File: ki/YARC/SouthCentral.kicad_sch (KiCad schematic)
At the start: 9 parts, among them U104 74LS86, U83 74LS139, U84 74LS157, U85 74LS157, U86 74LS157, U87 74LS138, U88 74HC00, U89 74LS157, U90 74LS157

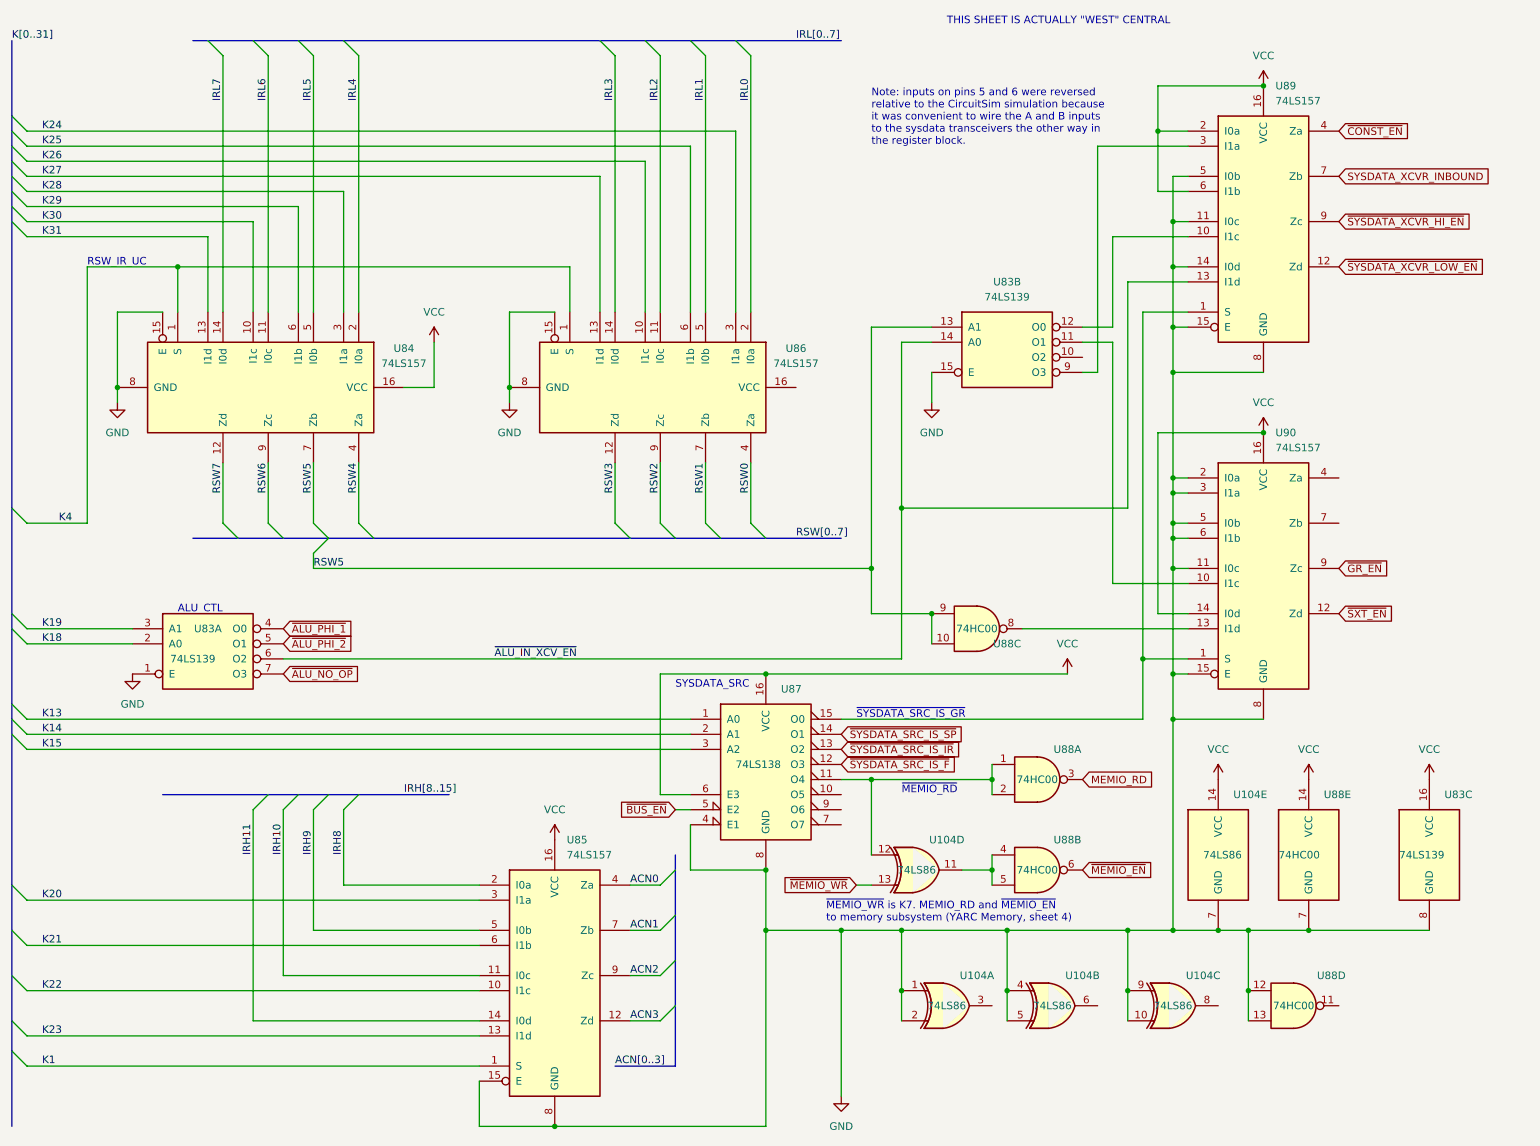
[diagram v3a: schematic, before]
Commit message: Ongoing fixes for ERC errors
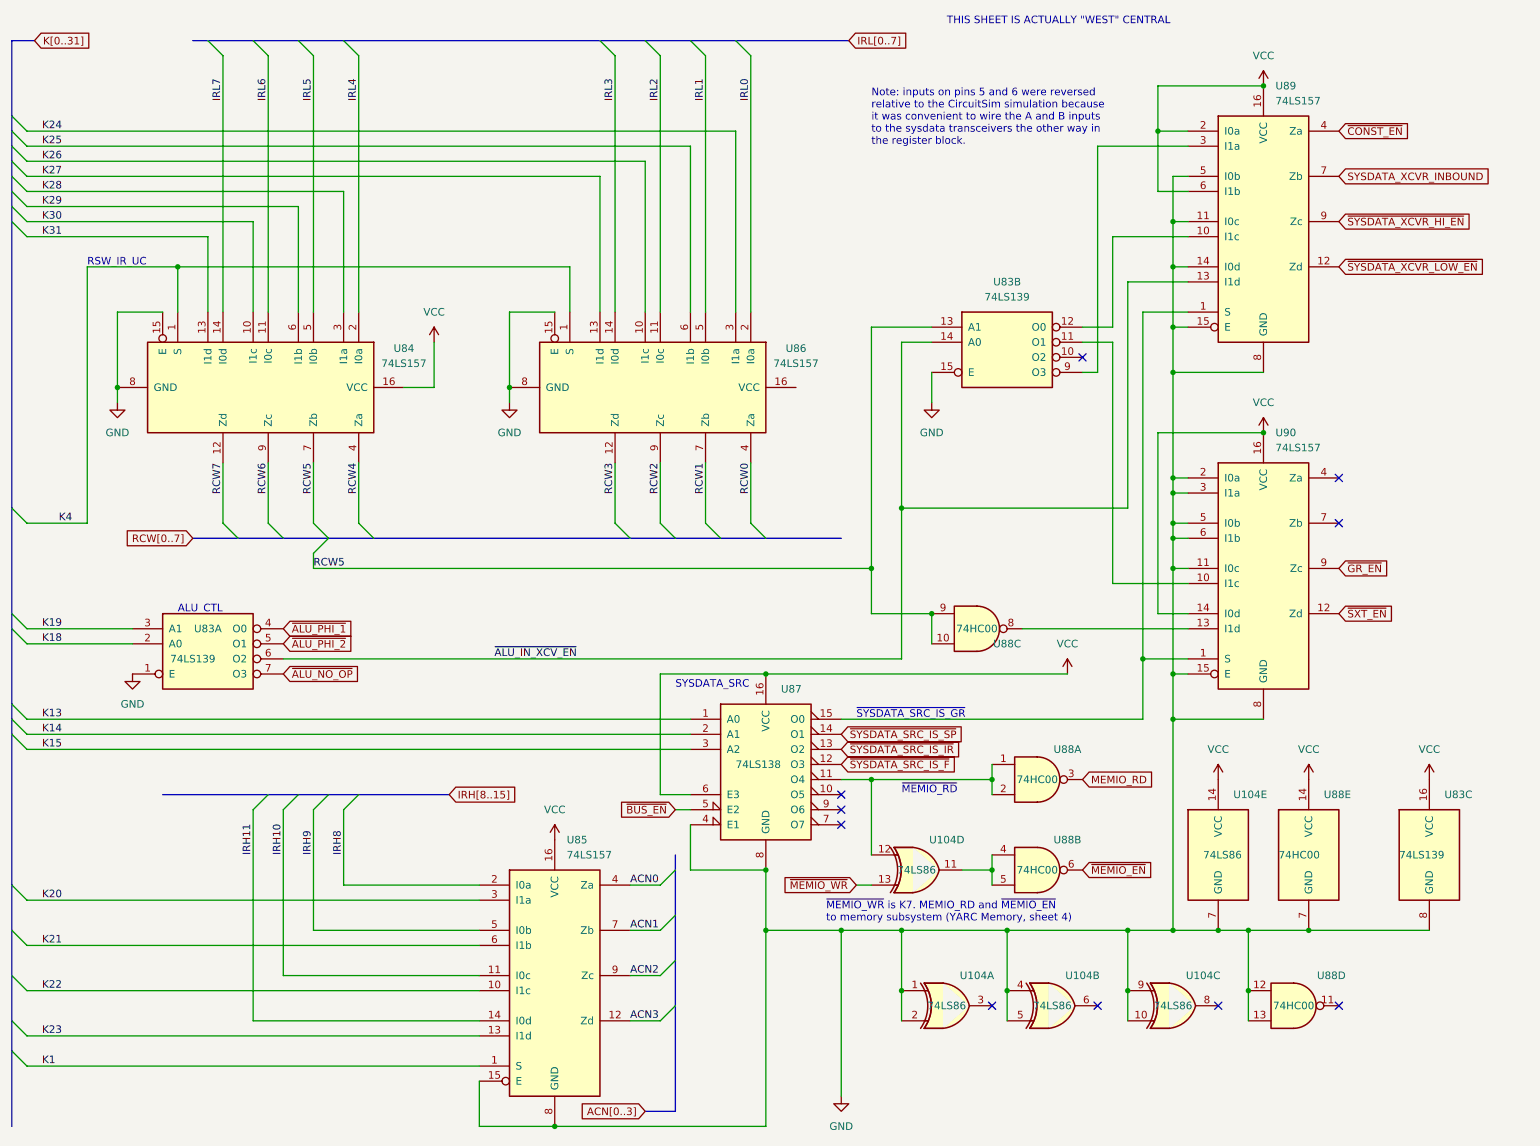
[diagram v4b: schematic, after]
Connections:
- net RSW0 renamed RCW0
- net RSW1 renamed RCW1
- net RSW2 renamed RCW2
- net RSW3 renamed RCW3
- net RSW4 renamed RCW4
- net RSW5 renamed RCW5
- net RSW6 renamed RCW6
- net RSW7 renamed RCW7
- no-connect marks 0 -> 10
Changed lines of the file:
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@@
   (junction (at 180.34 157.48) (diameter 0) (color 0 0 0 0)
   )
+  (no_connect (at 180.34 180.34))
+  (no_connect (at 238.76 91.44))
+  (no_connect (at 238.76 99.06))
+  (no_connect (at 195.58 71.12))
+  (no_connect (at 238.76 180.34))
+  (no_connect (at 154.94 147.32))
+  (no_connect (at 154.94 144.78))
+  (no_connect (at 198.12 180.34))
+  (no_connect (at 154.94 149.86))
+  (no_connect (at 218.44 180.34))
   (bus_entry (at 68.58 101.6) (size -2.54 -2.54)
     (stroke (width 0) (type default))
@@
     (stroke (width 0) (type default))
   )
-  (bus (pts (xy 116.84 190.5) (xy 127 190.5))
+  (bus (pts (xy 121.92 198.12) (xy 127 198.12))
     (stroke (width 0) (type default))
   )
@@
     (stroke (width 0) (type default))
   )
-  (bus (pts (xy 127 180.34) (xy 127 190.5))
+  (bus (pts (xy 127 180.34) (xy 127 198.12))
     (stroke (width 0) (type default))
   )
@@
     (stroke (width 0) (type default))
   )
+  (bus (pts (xy 15.24 17.78) (xy 19.05 17.78))
+    (stroke (width 0) (type default))
+  )
   (wire (pts (xy 33.02 78.74) (xy 33.02 76.2))
     (stroke (width 0) (type default))
@@
     (stroke (width 0) (type default))
   )
-  (bus (pts (xy 137.16 17.78) (xy 154.94 17.78))
+  (bus (pts (xy 137.16 17.78) (xy 156.21 17.78))
     (stroke (width 0) (type default))
   )
@@
     (effects (font (size 1.27 1.27)) (justify left bottom))
   )
-  (label "RSW6" (at 58.42 88.9 270) (fields_autoplaced)
+  (label "RCW6" (at 58.42 88.9 270) (fields_autoplaced)
     (effects (font (size 1.27 1.27)) (justify right bottom))
   )
@@
     (effects (font (size 1.27 1.27)) (justify left bottom))
   )
-  (label "RSW2" (at 124.46 88.9 270) (fields_autoplaced)
+  (label "RCW2" (at 124.46 88.9 270) (fields_autoplaced)
     (effects (font (size 1.27 1.27)) (justify right bottom))
   )
@@
   )
   (label "IRL0" (at 139.7 27.94 90) (fields_autoplaced)
-    (effects (font (size 1.27 1.27)) (justify left bottom))
-  )
-  (label "RSW[0..7]" (at 147.32 101.6 0) (fields_autoplaced)
     (effects (font (size 1.27 1.27)) (justify left bottom))
   )
@@
     (effects (font (size 1.27 1.27)) (justify right bottom))
   )
-  (label "K[0..31]" (at 15.24 17.78 0) (fields_autoplaced)
-    (effects (font (size 1.27 1.27)) (justify left bottom))
-  )
   (label "~{ALU_IN_XCV_EN}" (at 96.52 121.92 0) (fields_autoplaced)
     (effects (font (size 1.27 1.27)) (justify left bottom))
@@
     (effects (font (size 1.27 1.27)) (justify left bottom))
   )
-  (label "RSW0" (at 139.7 88.9 270) (fields_autoplaced)
+  (label "RCW0" (at 139.7 88.9 270) (fields_autoplaced)
     (effects (font (size 1.27 1.27)) (justify right bottom))
   )
@@
     (effects (font (size 1.27 1.27)) (justify left bottom))
   )
-  (label "ACN[0..3]" (at 116.84 190.5 0) (fields_autoplaced)
-    (effects (font (size 1.27 1.27)) (justify left bottom))
-  )
-  (label "RSW3" (at 116.84 88.9 270) (fields_autoplaced)
+  (label "RCW3" (at 116.84 88.9 270) (fields_autoplaced)
     (effects (font (size 1.27 1.27)) (justify right bottom))
   )
@@
     (effects (font (size 1.27 1.27)) (justify left bottom))
   )
-  (label "RSW7" (at 50.8 88.9 270) (fields_autoplaced)
+  (label "RCW7" (at 50.8 88.9 270) (fields_autoplaced)
     (effects (font (size 1.27 1.27)) (justify right bottom))
   )
@@
     (effects (font (size 1.27 1.27)) (justify left bottom))
   )
-  (label "IRH[8..15]" (at 81.28 144.78 0) (fields_autoplaced)
-    (effects (font (size 1.27 1.27)) (justify left bottom))
-  )
   (label "K24" (at 20.32 33.02 0) (fields_autoplaced)
     (effects (font (size 1.27 1.27)) (justify left bottom))
   )
-  (label "RSW1" (at 132.08 88.9 270) (fields_autoplaced)
+  (label "RCW1" (at 132.08 88.9 270) (fields_autoplaced)
     (effects (font (size 1.27 1.27)) (justify right bottom))
   )
@@
     (effects (font (size 1.27 1.27)) (justify left bottom))
   )
-  (label "RSW5" (at 66.04 88.9 270) (fields_autoplaced)
+  (label "RCW5" (at 66.04 88.9 270) (fields_autoplaced)
     (effects (font (size 1.27 1.27)) (justify right bottom))
   )
@@
     (effects (font (size 1.27 1.27)) (justify left bottom))
   )
-  (label "RSW4" (at 73.66 88.9 270) (fields_autoplaced)
+  (label "RCW4" (at 73.66 88.9 270) (fields_autoplaced)
     (effects (font (size 1.27 1.27)) (justify right bottom))
   )
@@
     (effects (font (size 1.27 1.27)) (justify left bottom))
   )
-  (label "IRL[0..7]" (at 147.32 17.78 0) (fields_autoplaced)
-    (effects (font (size 1.27 1.27)) (justify left bottom))
-  )
   (label "IRH11" (at 55.88 154.94 90) (fields_autoplaced)
     (effects (font (size 1.27 1.27)) (justify left bottom))
   )
-  (label "RSW5" (at 66.04 106.68 0) (fields_autoplaced)
+  (label "RCW5" (at 66.04 106.68 0) (fields_autoplaced)
     (effects (font (size 1.27 1.27)) (justify left bottom))
   )
@@
     )
   )
+  (global_label "IRL[0..7]" (shape input) (at 156.21 17.78 0) (fields_autoplaced)
+    (effects (font (size 1.27 1.27)) (justify left))
+    (property "Intersheetrefs" "${INTERSHEET_REFS}" (at 167.4201 17.78 0)
+      (effects (font (size 1.27 1.27)) (justify left) hide)
+    )
+  )
   (global_label "MEMIO_RD" (shape input) (at 195.58 142.24 0) (fields_autoplaced)
     (effects (font (size 1.27 1.27)) (justify left))
@@
     )
   )
+  (global_label "IRH[8..15]" (shape input) (at 88.9 144.78 0) (fields_autoplaced)
+    (effects (font (size 1.27 1.27)) (justify left))
+    (property "Intersheetrefs" "${INTERSHEET_REFS}" (at 101.622 144.78 0)
+      (effects (font (size 1.27 1.27)) (justify left) hide)
+    )
+  )
   (global_label "~{SYSDATA_XCVR_HI_EN}" (shape input) (at 238.76 48.26 0) (fields_autoplaced)
     (effects (font (size 1.27 1.27)) (justify left))
@@
     (property "Intersheetrefs" "${INTERSHEET_REFS}" (at 207.4274 157.4006 0)
       (effects (font (size 1.27 1.27)) (justify left) hide)
+    )
+  )
+  (global_label "RCW[0..7]" (shape input) (at 45.72 101.6 180) (fields_autoplaced)
+    (effects (font (size 1.27 1.27)) (justify right))
+    (property "Intersheetrefs" "${INTERSHEET_REFS}" (at 33.4214 101.6 0)
+      (effects (font (size 1.27 1.27)) (justify right) hide)
+    )
+  )
+  (global_label "ACN[0..3]" (shape input) (at 121.92 198.12 180) (fields_autoplaced)
+    (effects (font (size 1.27 1.27)) (justify right))
+    (property "Intersheetrefs" "${INTERSHEET_REFS}" (at 109.9237 198.12 0)
+      (effects (font (size 1.27 1.27)) (justify right) hide)
     )
   )
@@
       (effects (font (size 1.27 1.27)) (justify left) hide)
     )
+  )
+  (global_label "K[0..31]" (shape input) (at 19.05 17.78 0) (fields_autoplaced)
+    (effects (font (size 1.27 1.27)) (justify left))
+    (property "Intersheetrefs" "${INTERSHEET_REFS}" (at 29.8367 17.78 0)
+      (effects (font (size 1.27 1.27)) (justify left) hide)
+    )

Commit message: Ongoing schematic changes
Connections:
- net VCC: now also U86.16 (VCC)
- net RCW0 renamed DST:0
- net RCW1 renamed DST:1
- net RCW2 renamed DST:2
- net RCW3 renamed SRC2:0
- net RCW4 renamed SRC2:1
- net RCW5 renamed SRC2:2
- net RCW6 renamed SRC1:0
- net RCW7 renamed SRC1:1
- net ~{SYSDATA_SRC_IS_SP} renamed ~{SYSDATA_SRC_IS_A}

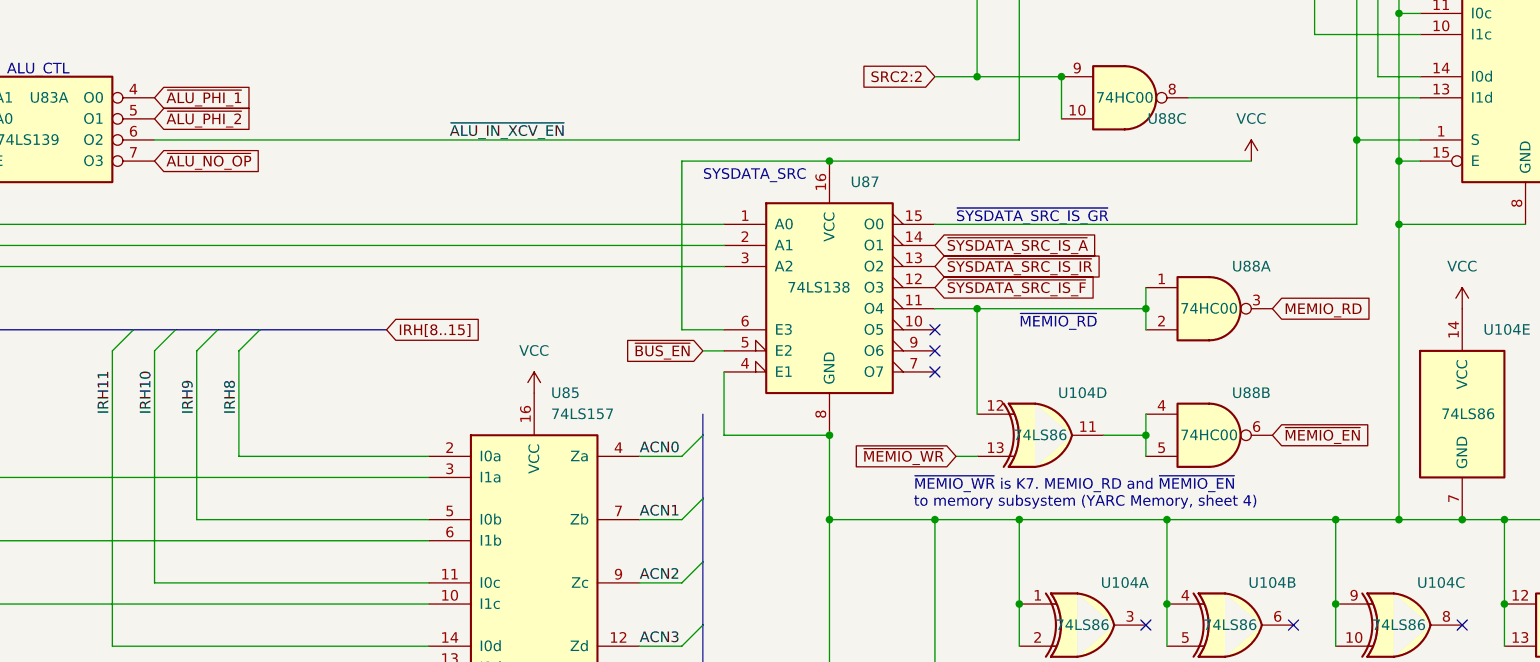
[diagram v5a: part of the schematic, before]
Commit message: Schematic for addressing unit is complete and all ERC violations addressed
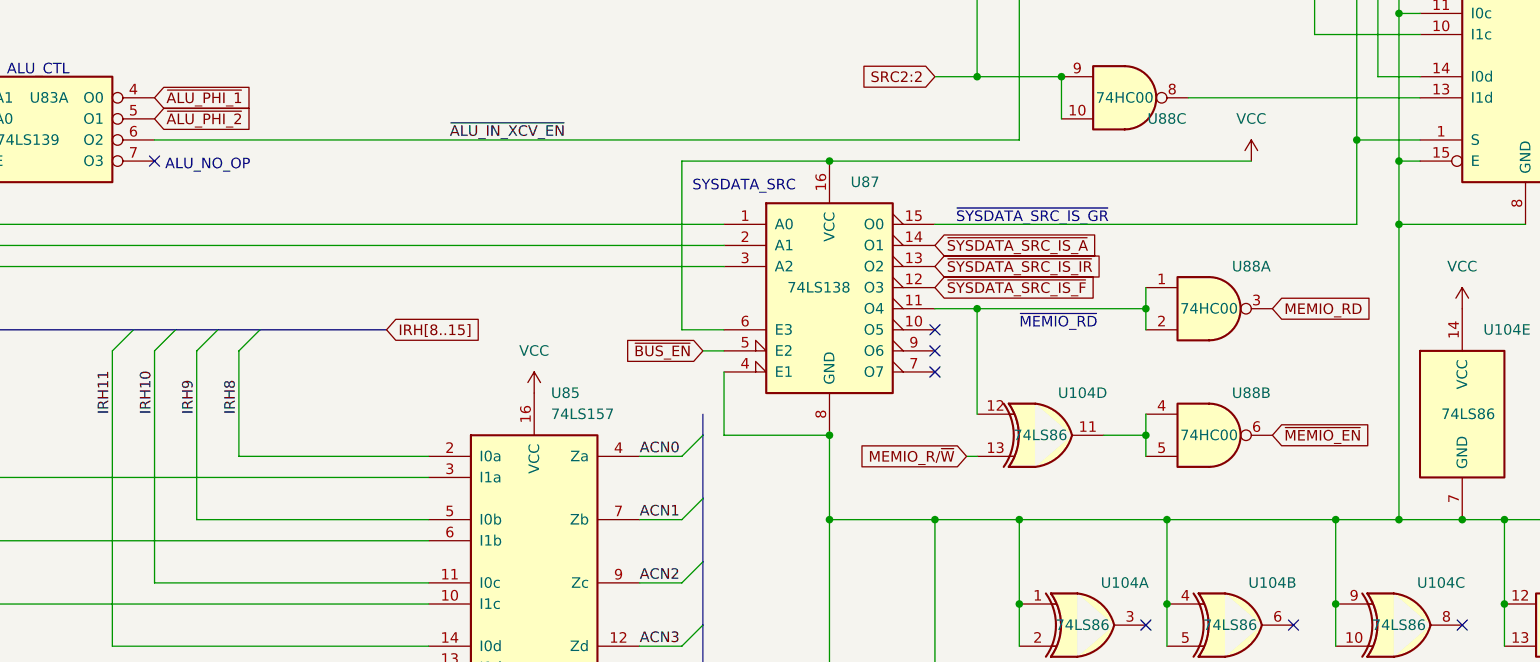
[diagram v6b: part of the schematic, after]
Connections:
- net ~{ALU_NO_OP}: no longer names the net of U83.7 (O3)
- net ~{MEMIO_WR} renamed MEMIO_R/~{W}
- no-connect marks 10 -> 11
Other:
- note added: "ALU_NO_OP"
- note removed: "~{MEMIO_WR} is K7. MEMIO_RD and ~{MEMIO_EN} to memory subsystem (YARC Memory, sheet 4)"
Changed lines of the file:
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@@
   (junction (at 180.34 157.48) (diameter 0) (color 0 0 0 0)
   )
+  (no_connect (at 60.96 124.46))
   (no_connect (at 180.34 180.34))
   (no_connect (at 238.76 91.44))
@@
     (stroke (width 0) (type default))
   )
-  (wire (pts (xy 160.02 160.02) (xy 157.48 160.02))
+  (wire (pts (xy 160.02 160.02) (xy 158.75 160.02))
     (stroke (width 0) (type default))
   )
@@
     (effects (font (size 1.27 1.27)) (justify left bottom))
   )
+  (text "ALU_NO_OP" (at 62.23 125.73 0)
+    (effects (font (size 1.27 1.27)) (justify left bottom))
+  )
   (text "ALU_CTL" (at 43.18 114.3 0)
     (effects (font (size 1.27 1.27)) (justify left bottom))
@@
   )
   (text "RSW_IR_UC" (at 27.94 55.88 0)
-    (effects (font (size 1.27 1.27)) (justify left bottom))
-  )
-  (text "~{MEMIO_WR} is K7. MEMIO_RD and ~{MEMIO_EN}\nto memory subsystem (YARC Memory, sheet 4)"
-    (at 152.4 166.37 0)
     (effects (font (size 1.27 1.27)) (justify left bottom))
   )
@@
     (effects (font (size 1.27 1.27)) (justify left bottom))
   )
-  (text "SYSDATA_SRC" (at 127 127 0)
+  (text "SYSDATA_SRC" (at 125.73 128.27 0)
     (effects (font (size 1.27 1.27)) (justify left bottom))
   )
@@
     )
   )
-  (global_label "~{ALU_NO_OP}" (shape input) (at 60.96 124.46 0) (fields_autoplaced)
-    (effects (font (size 1.27 1.27)) (justify left))
-    (property "Intersheetrefs" "${INTERSHEET_REFS}" (at 74.0169 124.3806 0)
-      (effects (font (size 1.27 1.27)) (justify left) hide)
-    )
-  )
   (global_label "SRC2:2" (shape input) (at 154.94 114.3 180) (fields_autoplaced)
     (effects (font (size 1.27 1.27)) (justify right))
@@
     )
   )
-  (global_label "~{MEMIO_WR}" (shape input) (at 157.48 160.02 180) (fields_autoplaced)
-    (effects (font (size 1.27 1.27)) (justify right))
-    (property "Intersheetrefs" "${INTERSHEET_REFS}" (at 145.3907 159.9406 0)
+  (global_label "MEMIO_R{slash}~{W}" (shape input) (at 158.75 160.02 180) (fields_autoplaced)
+    (effects (font (size 1.27 1.27)) (justify right))
+    (property "Intersheetrefs" "${INTERSHEET_REFS}" (at 144.7582 160.02 0)
       (effects (font (size 1.27 1.27)) (justify right) hide)
     )
@@
   (global_label "SYSDATA_XCVR_INBOUND" (shape input) (at 238.76 40.64 0) (fields_autoplaced)
     (effects (font (size 1.27 1.27)) (justify left))
-    (property "Intersheetrefs" "${INTERSHEET_REFS}" (at 264.3355 40.5606 0)
-      (effects (font (size 1.27 1.27)) (justify left) hide)
-    )
+    (property "Intersheetrefs" "${INTERSHEET_REFS}" (at 264.9077 40.64 0)
+      (effects (font (size 1.27 1.27)) (justify left) hide)
+    )
